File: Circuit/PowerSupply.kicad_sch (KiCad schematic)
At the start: 1 part

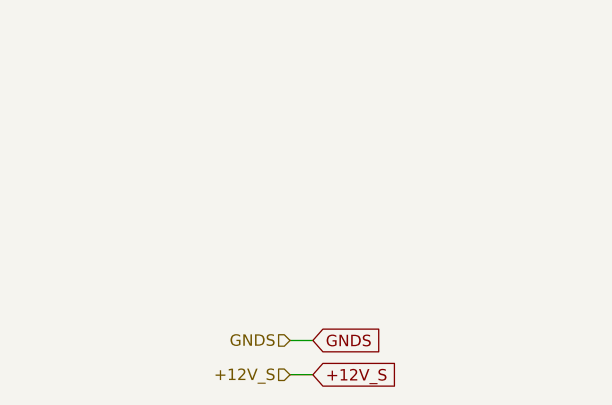
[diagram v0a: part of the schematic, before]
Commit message: SMUの各部分の配線を追加
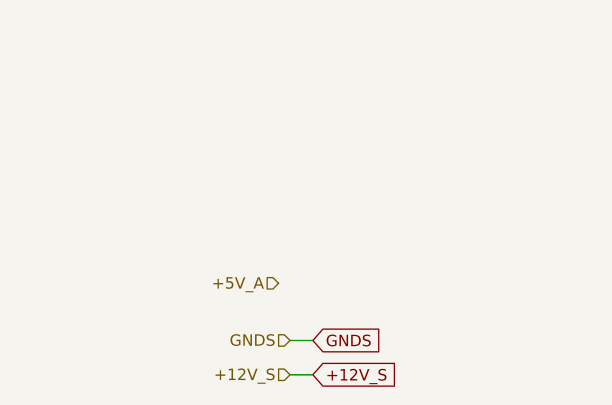
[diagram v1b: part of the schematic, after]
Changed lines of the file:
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@@
+		)
+	)
+	(hierarchical_label "+5V_A"
+		(shape input)
+		(at 57.15 139.7 180)
+		(fields_autoplaced yes)
+		(effects
+			(font
+				(size 1.27 1.27)
+			)
+			(justify right)
 		)
 	)
